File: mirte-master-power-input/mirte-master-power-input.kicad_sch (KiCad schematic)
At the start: 3 parts, among them J1 pwr_in, J2 battery, J3 robot

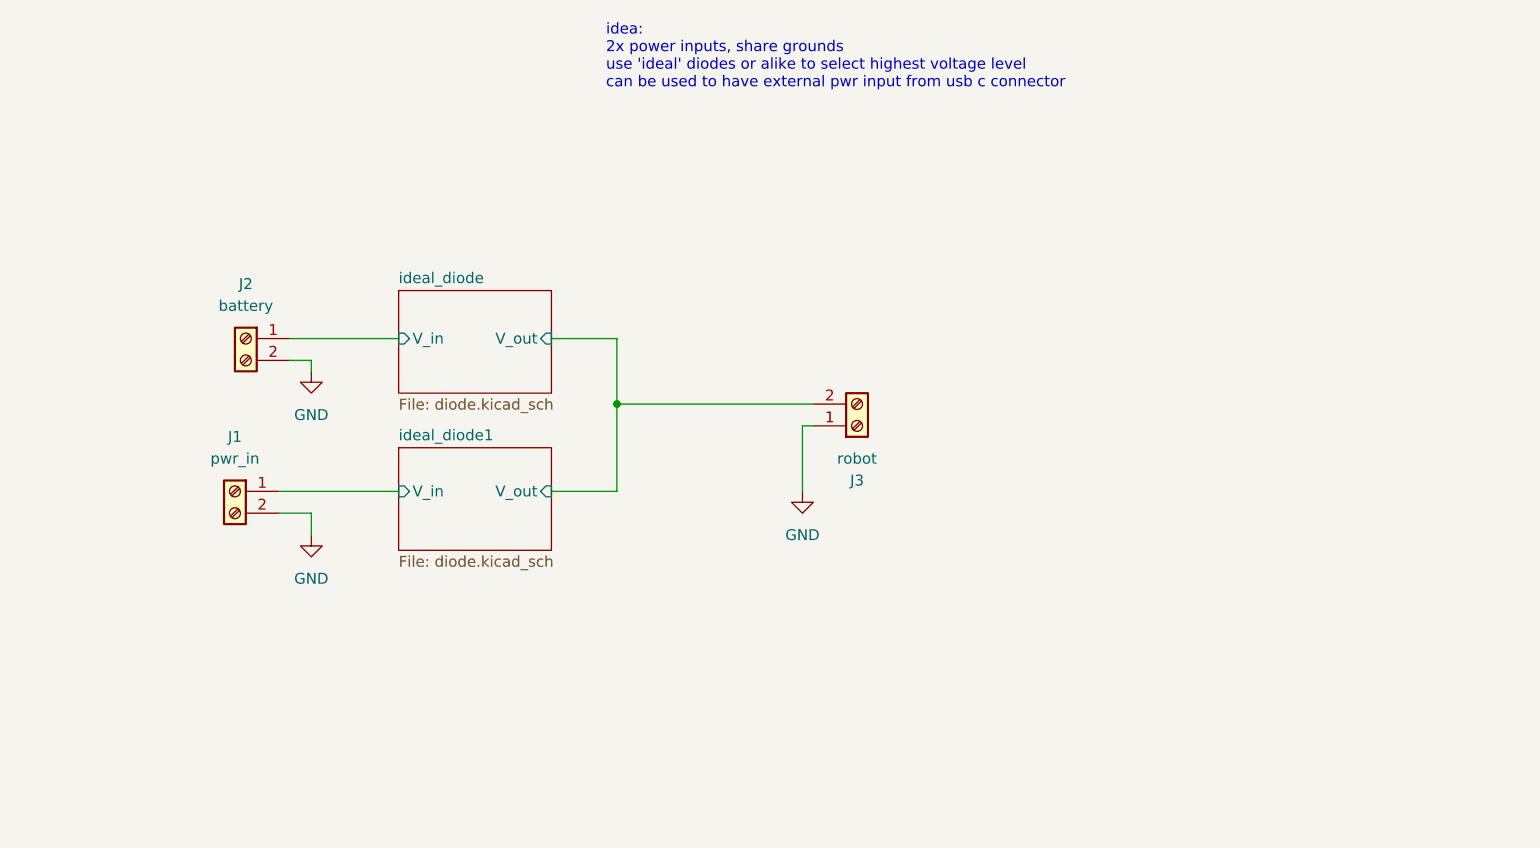
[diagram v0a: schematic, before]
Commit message: Power input: fix layout & fix diode setup
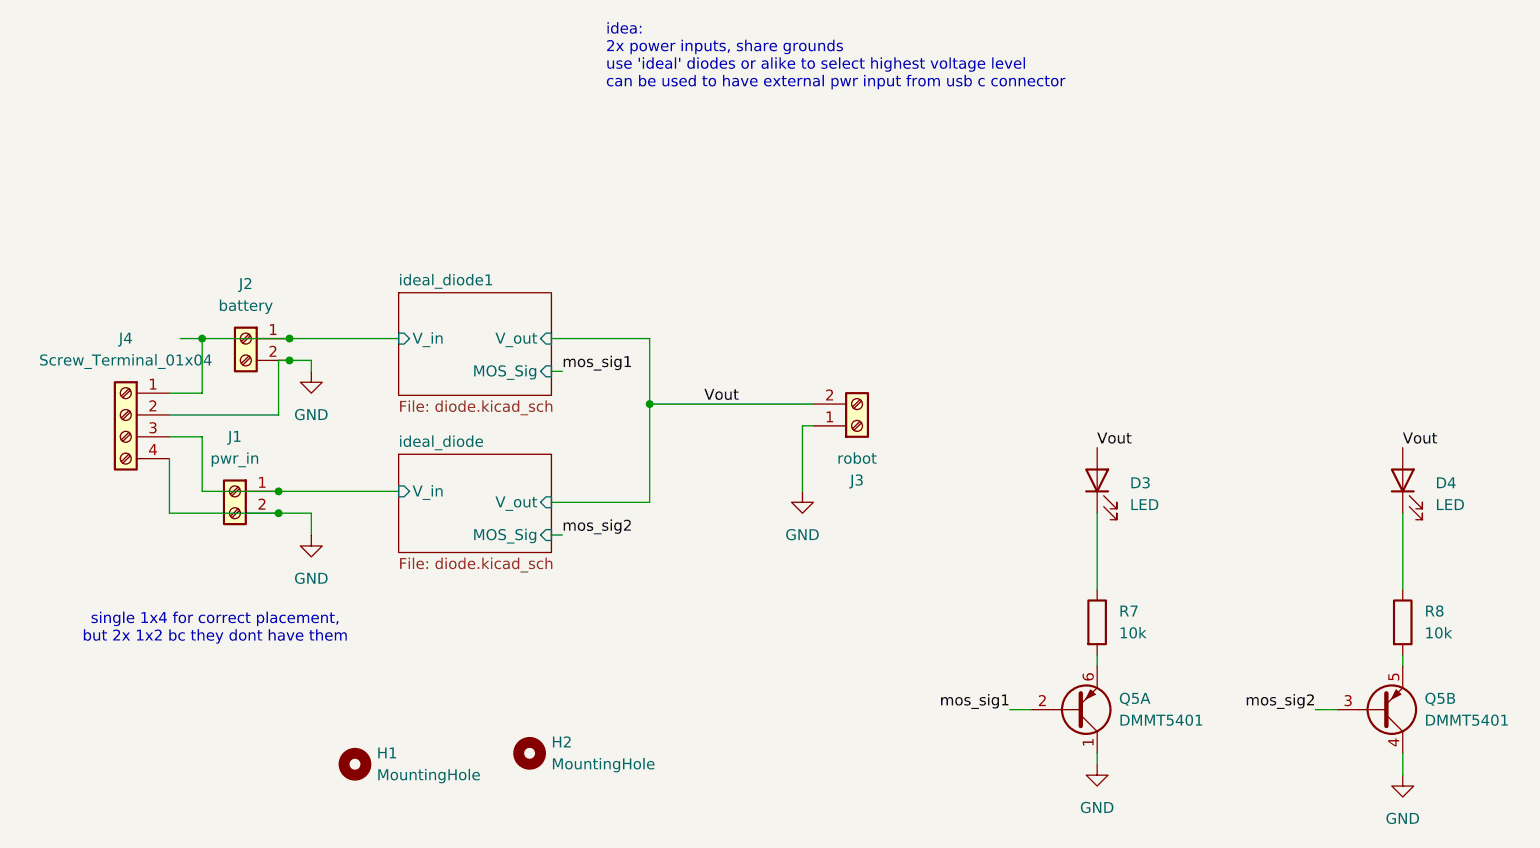
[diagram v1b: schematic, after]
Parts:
- added D3, D4: LED, LED_SMD:LED_0805_2012Metric, symbol Device:LED
- added H1, H2: MountingHole, MountingHole:MountingHole_3.2mm_M3, symbol Mechanical:MountingHole
- added J4: Screw_Terminal_01x04, TerminalBlock_Phoenix:TerminalBlock_Phoenix_PT-1,5-4-5.0-H_1x04_P5.00mm_Horizontal, symbol Connector:Screw_Terminal_01x04
- added Q5: DMMT5401, Package_TO_SOT_SMD:SOT-23-6, symbol Transistor_BJT:DMMT5401
- added R7, R8: 10k, Resistor_SMD:R_0805_2012Metric, symbol Device:R
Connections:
- net GND: now also J4.2 (Pin_2), J4.4 (Pin_4), Q5.1 (C1), Q5.4 (C2)
- net ideal_diode/V_in: now also J1.1 (Pin_1), J4.3 (Pin_3); no longer J2.1 (Pin_1)
- net ideal_diode1/V_in: now also J2.1 (Pin_1), J4.1 (Pin_1); no longer J1.1 (Pin_1)
- net ideal_diode/V_out renamed Vout
- net Vout: now also D3.2 (A), D4.2 (A)
- new net: D3.1 (K), R7.1
- new net: Q5.6 (E1), R7.2
- new net: Q5.5 (E2), R8.2
- new net: D4.1 (K), R8.1
- new net mos_sig1: Q5.2 (B1)
- new net mos_sig2: Q5.3 (B2)
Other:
- sheet ideal_diode ports: added MOS_Sig; removed none
- sheet ideal_diode1 ports: added MOS_Sig; removed none
- note added: "single 1x4 for correct placement, but 2x 1x2 bc they dont have them"
